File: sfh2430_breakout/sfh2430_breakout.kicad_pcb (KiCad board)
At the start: 2 copper layers, 45 x 60.3 mm, 118 parts, among them J1 Landing Pad, J10 Conn_01x01, J11 Conn_01x01, J12 Conn_01x01, J13 Conn_01x01, J2 Landing Pad, J3 Landing Pad, J4 Landing Pad, J5 Conn_01x10, J6 Conn_01x01, J7 Conn_01x01, J8 Conn_01x01, J9 Conn_01x01, U1 LTC2052IS_PBF

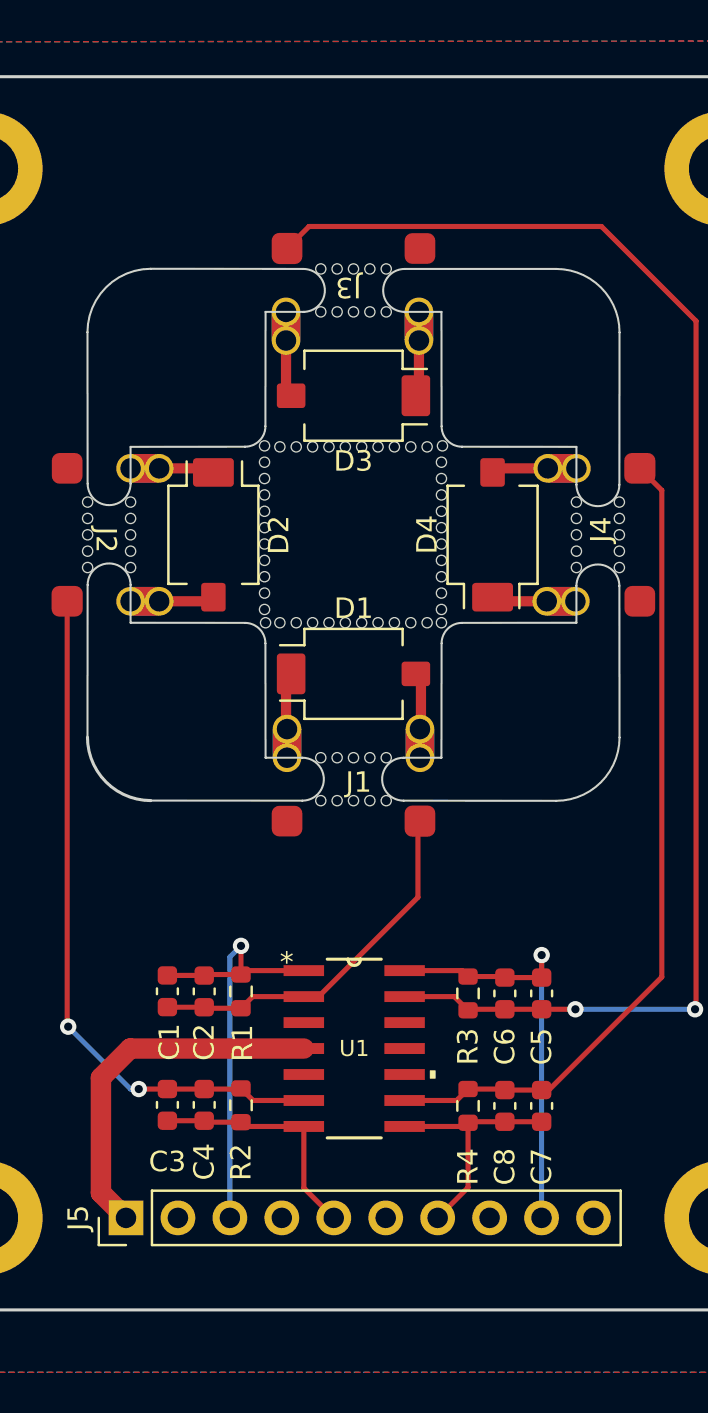
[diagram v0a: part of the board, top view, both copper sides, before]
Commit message: add math and decals
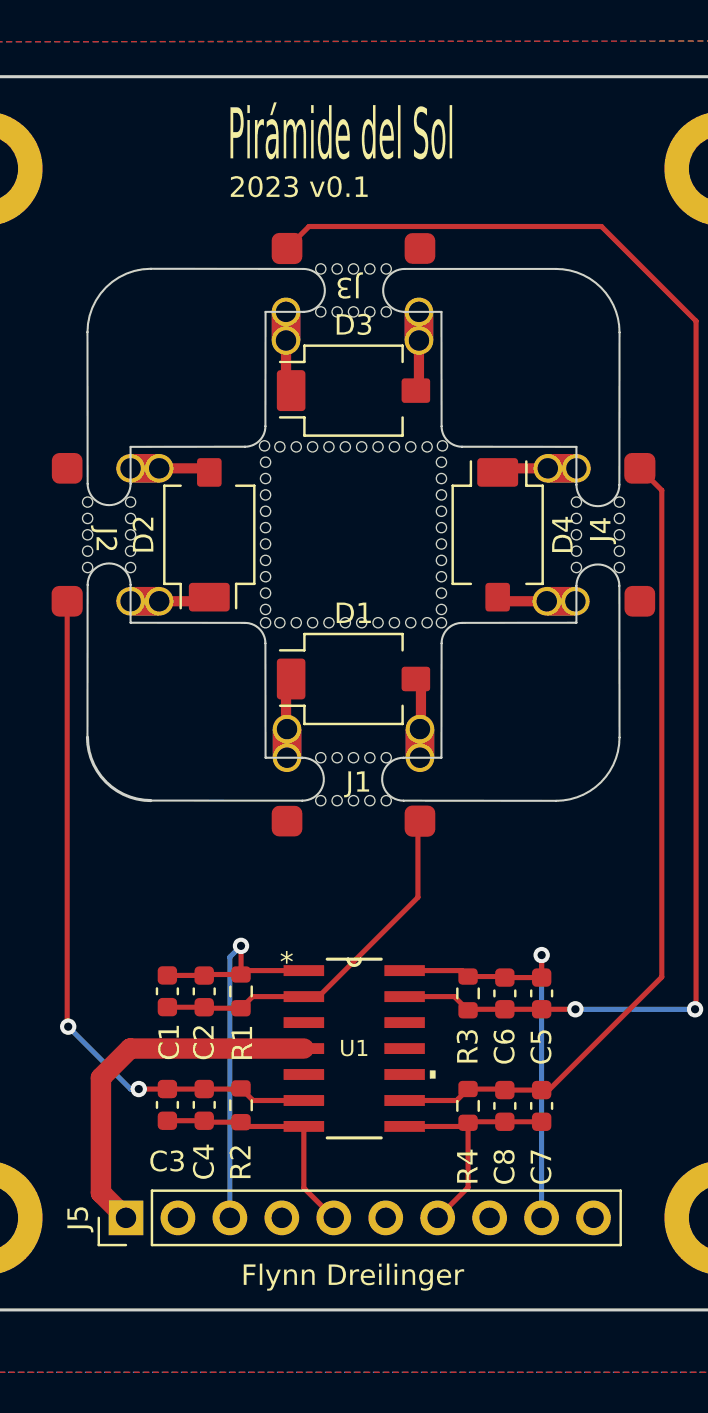
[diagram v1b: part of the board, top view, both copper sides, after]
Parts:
- added G***: LOGO, adcs:2ducks, B.Cu at (91.7, 67.8)
- added G***: LOGO, adcs:unlimited_ducks_2, B.Cu at (73.2, 51.9)
- added G***: LOGO, adcs:sats_pro_shop, B.Cu at (73.0, 91.0)
- added G***: LOGO, adcs:2ducks, B.Cu at (54.1, 68.2)
- R1, R2, R3, R4: value 1M -> 3.9k
- moved D1 0.25 mm to (72.8, 75.8)
- moved D3 0.25 mm to (72.8, 61.6), turned to 0 degrees
- moved D4 0.25 mm to (79.8, 68.7), turned to -90 degrees
- moved D2 0.20 mm to (65.8, 68.7), turned to 90 degrees
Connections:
- J10 pad 1: Net-(D3-A) -> Net-(D3-K)
- J11 pad 1: Net-(D3-K) -> Net-(D3-A)
- J12 pad 1: Net-(D4-A) -> Net-(D4-K)
- J13 pad 1: Net-(D4-K) -> Net-(D4-A)
- J6 pad 1: Net-(D1-A) -> Net-(D1-K)
- J7 pad 1: Net-(D1-K) -> Net-(D1-A)
- J8 pad 1: Net-(D2-A) -> Net-(D2-K)
- J9 pad 1: Net-(D2-K) -> Net-(D2-A)
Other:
- board text added: "2023 v0.1"
- board text added: "Flynn Dreilinger"
- board text added: "Pirámide del Sol"

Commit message: ordered sfh2430 breakout rev 0.1
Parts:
- removed the REF** at (74.4, 79.6)
- removed the REF** at (74.4, 57.8)
- removed the REF** at (77.1, 70.0)
- removed the REF** at (85.8, 67.9)
- removed the REF** at (71.2, 57.8)
- removed the REF** at (74.4, 81.7)
- removed the REF** at (77.1, 73.0)
- removed the REF** at (72.0, 55.7)
- removed the REF** at (76.4, 73.0)
- removed the REF** at (74.0, 64.4)
- removed the REF** at (77.1, 68.3)
- removed the REF** at (73.2, 64.4)
- removed the REF** at (69.2, 64.4)
- removed the REF** at (68.5, 70.8)
- removed the REF** at (68.5, 65.2)
- removed the REF** at (83.7, 67.9)
- removed the REF** at (75.6, 73.0)
- removed the REF** at (61.9, 69.5)
- removed the REF** at (70.0, 73.0)
- removed the REF** at (85.8, 69.5)
- removed the REF** at (73.6, 55.7)
- removed the REF** at (85.8, 67.1)
- removed the REF** at (73.2, 73.0)
- removed the REF** at (72.8, 57.8)
- removed the REF** at (68.5, 71.5)
- removed the REF** at (73.6, 81.7)
- removed the REF** at (68.5, 69.2)
- removed the REF** at (68.5, 66.0)
- removed the REF** at (72.4, 73.0)
- removed the REF** at (77.1, 66.0)
- removed the REF** at (61.9, 67.1)
- removed the REF** at (59.8, 69.5)
- removed the REF** at (70.0, 64.4)
- removed the REF** at (71.2, 79.6)
- removed the REF** at (71.6, 73.0)
- removed the REF** at (72.0, 79.6)
- removed the REF** at (77.2, 64.3)
- removed the REF** at (68.5, 72.3)
- removed the REF** at (71.2, 55.7)
- removed the REF** at (61.9, 70.3)
- removed the REF** at (77.1, 67.5)
- removed the REF** at (68.5, 70.0)
- removed the REF** at (72.0, 81.7)
- removed the REF** at (77.1, 66.8)
- removed the REF** at (77.1, 69.2)
- removed the REF** at (70.8, 64.4)
- removed the REF** at (73.6, 57.8)
- removed the REF** at (59.8, 67.1)
- removed the REF** at (68.5, 68.3)
- removed the REF** at (59.8, 70.3)
- removed the REF** at (74.0, 73.0)
- removed the REF** at (85.8, 70.3)
- removed the REF** at (83.7, 69.5)
- removed the REF** at (72.4, 64.4)
- removed the REF** at (77.1, 70.8)
- removed the REF** at (75.6, 64.4)
- removed the REF** at (70.8, 73.0)
- removed the REF** at (61.9, 68.7)
- removed the REF** at (68.5, 67.5)
- removed the REF** at (74.4, 55.7)
- removed the REF** at (71.6, 64.4)
- removed the REF** at (77.1, 72.3)
- removed the REF** at (59.8, 68.7)
- removed the REF** at (59.8, 67.9)
- removed the REF** at (83.7, 68.7)
- removed the REF** at (72.8, 81.7)
- removed the REF** at (72.8, 55.7)
- removed the REF** at (69.2, 73.0)
- removed the REF** at (73.6, 79.6)
- removed the REF** at (74.8, 73.0)
- removed the REF** at (68.5, 73.0)
- removed the REF** at (68.5, 66.8)
- removed the REF** at (72.0, 57.8)
- removed the REF** at (85.8, 68.7)
- removed the REF** at (61.9, 67.9)
- removed the REF** at (76.4, 64.4)
- removed the REF** at (83.7, 67.1)
- removed the REF** at (74.8, 64.4)
- removed the REF** at (71.2, 81.7)
- removed the REF** at (77.1, 65.2)
- removed the REF** at (83.7, 70.3)
- removed the REF** at (68.5, 64.3)
- removed the REF** at (77.1, 71.5)
- removed the REF** at (72.8, 79.6)
- added REF**: NPTH, NPTH, F.Cu at (87.0, 106.7)
- added REF**: NPTH, NPTH, F.Cu at (72.8, 115.7)
- added REF**: NPTH, NPTH, F.Cu at (66.7, 109.4)
- added REF**: NPTH, NPTH, F.Cu at (82.5, 114.9)
- added REF**: NPTH, NPTH, F.Cu at (75.7, 106.7)
- added REF**: NPTH, NPTH, F.Cu at (60.2, 106.7)
- added REF**: NPTH, NPTH, F.Cu at (58.6, 109.4)
- added REF**: NPTH, NPTH, F.Cu at (77.2, 106.7)
- added REF**: NPTH, NPTH, F.Cu at (63.1, 110.0)
- added REF**: NPTH, NPTH, F.Cu at (61.0, 106.7)
- added REF**: NPTH, NPTH, F.Cu at (77.2, 109.4)
- added REF**: NPTH, NPTH, F.Cu at (68.3, 109.4)
- added REF**: NPTH, NPTH, F.Cu at (79.7, 106.7)
- added REF**: NPTH, NPTH, F.Cu at (57.0, 109.4)
- added REF**: NPTH, NPTH, F.Cu at (84.5, 106.7)
- added REF**: NPTH, NPTH, F.Cu at (63.1, 114.8)
- added REF**: NPTH, NPTH, F.Cu at (87.8, 106.7)
- added REF**: NPTH, NPTH, F.Cu at (89.3, 106.7)
- added REF**: NPTH, NPTH, F.Cu at (78.8, 106.7)
- added REF**: NPTH, NPTH, F.Cu at (67.5, 109.4)
- added REF**: NPTH, NPTH, F.Cu at (72.8, 110.9)
- added REF**: NPTH, NPTH, F.Cu at (58.6, 106.7)
- added REF**: NPTH, NPTH, F.Cu at (82.5, 115.7)
- added REF**: NPTH, NPTH, F.Cu at (82.5, 110.9)
- added REF**: NPTH, NPTH, F.Cu at (76.4, 109.4)
- added REF**: NPTH, NPTH, F.Cu at (79.6, 109.4)
- added REF**: NPTH, NPTH, F.Cu at (90.2, 106.7)
- added REF**: NPTH, NPTH, F.Cu at (66.8, 106.7)
- added REF**: NPTH, NPTH, F.Cu at (84.5, 109.5)
- added REF**: NPTH, NPTH, F.Cu at (86.9, 109.5)
- added REF**: NPTH, NPTH, F.Cu at (82.5, 113.3)
- added REF**: NPTH, NPTH, F.Cu at (60.2, 109.4)
- added REF**: NPTH, NPTH, F.Cu at (63.1, 114.0)
- added REF**: NPTH, NPTH, F.Cu at (63.1, 111.6)
- added REF**: NPTH, NPTH, F.Cu at (57.8, 109.4)
- added REF**: NPTH, NPTH, F.Cu at (82.5, 110.1)
- added REF**: NPTH, NPTH, F.Cu at (85.3, 109.5)
- added REF**: NPTH, NPTH, F.Cu at (72.8, 114.9)
- added REF**: NPTH, NPTH, F.Cu at (69.9, 109.4)
- added REF**: NPTH, NPTH, F.Cu at (74.8, 109.4)
- added REF**: NPTH, NPTH, F.Cu at (69.2, 106.7)
- added REF**: NPTH, NPTH, F.Cu at (57.0, 106.7)
- added REF**: NPTH, NPTH, F.Cu at (63.1, 113.2)
- added REF**: NPTH, NPTH, F.Cu at (57.9, 106.7)
- added REF**: NPTH, NPTH, F.Cu at (66.0, 106.7)
- added REF**: NPTH, NPTH, F.Cu at (72.8, 110.1)
- added REF**: NPTH, NPTH, F.Cu at (56.2, 106.7)
- added REF**: NPTH, NPTH, F.Cu at (55.5, 106.7)
- added REF**: NPTH, NPTH, F.Cu at (74.8, 106.7)
- added REF**: NPTH, NPTH, F.Cu at (65.2, 106.7)
- added REF**: NPTH, NPTH, F.Cu at (69.1, 109.4)
- added REF**: NPTH, NPTH, F.Cu at (68.3, 106.7)
- added REF**: NPTH, NPTH, F.Cu at (88.5, 106.7)
- added REF**: NPTH, NPTH, F.Cu at (86.2, 106.7)
- added REF**: NPTH, NPTH, F.Cu at (87.7, 109.5)
- added REF**: NPTH, NPTH, F.Cu at (72.8, 111.7)
- added REF**: NPTH, NPTH, F.Cu at (55.4, 109.4)
- added REF**: NPTH, NPTH, F.Cu at (72.8, 114.1)
- added REF**: NPTH, NPTH, F.Cu at (82.5, 114.1)
- added REF**: NPTH, NPTH, F.Cu at (78.0, 106.7)
- added REF**: NPTH, NPTH, F.Cu at (63.1, 110.8)
- added REF**: NPTH, NPTH, F.Cu at (59.5, 106.7)
- added REF**: NPTH, NPTH, F.Cu at (65.1, 109.4)
- added REF**: NPTH, NPTH, F.Cu at (59.4, 109.4)
- added REF**: NPTH, NPTH, F.Cu at (88.5, 109.5)
- added REF**: NPTH, NPTH, F.Cu at (70.0, 106.7)
- added REF**: NPTH, NPTH, F.Cu at (82.5, 111.7)
- added REF**: NPTH, NPTH, F.Cu at (61.0, 109.4)
- added REF**: NPTH, NPTH, F.Cu at (80.4, 109.4)
- added REF**: NPTH, NPTH, F.Cu at (63.1, 112.4)
- added REF**: NPTH, NPTH, F.Cu at (76.5, 106.7)
- added REF**: NPTH, NPTH, F.Cu at (63.1, 115.6)
- added REF**: NPTH, NPTH, F.Cu at (80.5, 106.7)
- added REF**: NPTH, NPTH, F.Cu at (56.2, 109.4)
- added REF**: NPTH, NPTH, F.Cu at (70.8, 106.7)
- added REF**: NPTH, NPTH, F.Cu at (70.7, 109.4)
- added REF**: NPTH, NPTH, F.Cu at (78.0, 109.4)
- added REF**: NPTH, NPTH, F.Cu at (90.1, 109.5)
- added REF**: NPTH, NPTH, F.Cu at (65.9, 109.4)
- added REF**: NPTH, NPTH, F.Cu at (86.1, 109.5)
- added REF**: NPTH, NPTH, F.Cu at (72.8, 112.5)
- added REF**: NPTH, NPTH, F.Cu at (89.3, 109.5)
- added REF**: NPTH, NPTH, F.Cu at (67.5, 106.7)
- added REF**: NPTH, NPTH, F.Cu at (78.8, 109.4)
- added REF**: NPTH, NPTH, F.Cu at (85.3, 106.7)
- added REF**: NPTH, NPTH, F.Cu at (75.6, 109.4)
- added REF**: NPTH, NPTH, F.Cu at (82.5, 112.5)
- added REF**: NPTH, NPTH, F.Cu at (72.8, 113.3)
- D1, D2, D3, D4: footprint OptoDevice:Osram_SFH2430 -> adcs:Osram_SFH2430
- moved J11 59.5 mm to (64.8, 116.2), turned to -90 degrees
- moved J10 58.4 mm to (71.2, 116.2), turned to -90 degrees
- moved D3 50.9 mm to (68.0, 112.3), turned to 180 degrees
- moved J12 50.8 mm to (80.9, 116.2), turned to -90 degrees
- moved J9 50.0 mm to (55.0, 114.8), turned to 90 degrees
- moved J13 45.2 mm to (74.4, 116.2), turned to -90 degrees
- moved D2 44.3 mm to (58.2, 112.3), turned to 180 degrees
- moved D4 43.7 mm to (77.7, 112.3), turned to 180 degrees
- moved J8 42.9 mm to (61.5, 114.8), turned to 90 degrees
- moved D1 39.4 mm to (87.3, 112.3), turned to 180 degrees
- moved J6 39.4 mm to (90.5, 114.8)
- moved J7 39.4 mm to (84.0, 114.8)
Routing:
- net GND: vias 0 -> 2
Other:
- board size 45 x 60.3 mm -> 45 x 69.9 mm
- board text added: "A"
- board text added: "B"
- board text added: "C"
- board text added: "D"

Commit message: sfh2400 v2 (flex PCB)
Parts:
- removed G*** (x2): LOGO, adcs:2ducks
- removed G***: LOGO, adcs:unlimited_ducks_2
- removed G***: LOGO, adcs:sats_pro_shop
- removed H3: MountingHole_Pad, MountingHole:MountingHole_3.2mm_M3_DIN965_Pad
- removed J10, J11, J12, J13, J6, J7, J8, J9: Conn_01x01, adcs:castellated_05mm
- removed J2, J3, J4: Landing Pad, adcs:photodiode_landing_pad
- removed J5: Conn_01x10, Connector_PinHeader_2.54mm:PinHeader_1x10_P2.54mm_Vertical
- removed REF** (x88): NPTH, NPTH
- added locked: MountingHole_Pad, MountingHole:MountingHole_2.2mm_M2_DIN965_Pad_TopBottom, F.Cu at (113.0, 94.0)
- H1, H2, H4: footprint MountingHole:MountingHole_3.2mm_M3_DIN965_Pad -> MountingHole:MountingHole_2.2mm_M2_DIN965_Pad_TopBottom
- J1: value Landing Pad -> Conn_01x06; footprint adcs:photodiode_landing_pad -> sapling:MOLEX_2053380006
- moved H1 57.1 mm to (92.2, 94.0)
- moved D3 54.9 mm to (122.3, 104.5), turned to -90 degrees
- moved J1 42.2 mm to (102.5, 112.7), turned to 180 degrees
- moved H2 38.6 mm to (92.2, 111.8)
- moved C3 32.1 mm to (94.9, 104.1)
- moved C1 32.0 mm to (94.9, 98.3)
- moved C4 31.7 mm to (96.3, 104.1)
- moved C2 31.7 mm to (96.3, 98.3)
- moved D1 31.6 mm to (102.5, 84.7), turned to 0 degrees
- moved R2 31.4 mm to (97.8, 104.1)
- moved R1 31.3 mm to (97.8, 98.3)
- moved U1 30.5 mm to (102.5, 101.2)
- moved R4 29.8 mm to (107.2, 104.1)
- moved R3 29.7 mm to (107.2, 98.3)
- moved C8 29.4 mm to (108.7, 104.1)
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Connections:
- C1 pad 1: Net-(J1-Pin_2) -> /Photodiode 1/IN-
- C1 pad 2: /OUTA -> /OUT1
- C2 pad 1: Net-(J1-Pin_2) -> /Photodiode 1/IN-
- C2 pad 2: /OUTA -> /OUT1
- C3 pad 1: Net-(J2-Pin_2) -> /Photodiode 2/IN-
- C3 pad 2: /OUTB -> /OUT2
- C4 pad 1: Net-(J2-Pin_2) -> /Photodiode 2/IN-
- C4 pad 2: /OUTB -> /OUT2
- C5 pad 1: Net-(J3-Pin_2) -> /Photodiode 4/IN-
- C5 pad 2: /OUTD -> /OUT4
- C6 pad 1: Net-(J3-Pin_2) -> /Photodiode 4/IN-
- C6 pad 2: /OUTD -> /OUT4
- C7 pad 1: Net-(J4-Pin_2) -> /Photodiode 3/IN-
- C7 pad 2: /OUTC -> /OUT3
- C8 pad 1: Net-(J4-Pin_2) -> /Photodiode 3/IN-
- C8 pad 2: /OUTC -> /OUT3
- D1 pad 1: Net-(D1-K) -> /Photodiode 1/IN-
- D1 pad 2: Net-(D1-A) -> GND
- D2 pad 1: Net-(D2-K) -> /Photodiode 2/IN-
- D2 pad 2: Net-(D2-A) -> GND
- D3 pad 1: Net-(D3-K) -> /Photodiode 4/IN-
- D3 pad 2: Net-(D3-A) -> GND
- D4 pad 1: Net-(D4-K) -> /Photodiode 3/IN-
- D4 pad 2: Net-(D4-A) -> GND
- J1 pad 2: Net-(J1-Pin_2) -> /OUT2
- R1 pad 1: Net-(J1-Pin_2) -> /Photodiode 1/IN-
- R1 pad 2: /OUTA -> /OUT1
- R2 pad 1: Net-(J2-Pin_2) -> /Photodiode 2/IN-
- R2 pad 2: /OUTB -> /OUT2
- R3 pad 1: Net-(J3-Pin_2) -> /Photodiode 4/IN-
- R3 pad 2: /OUTD -> /OUT4
- R4 pad 1: Net-(J4-Pin_2) -> /Photodiode 3/IN-
- R4 pad 2: /OUTC -> /OUT3
- U1 pad 1: /OUTA -> /OUT1
- U1 pad 13: Net-(J3-Pin_2) -> /Photodiode 4/IN-
- U1 pad 14: /OUTD -> /OUT4
- U1 pad 2: Net-(J1-Pin_2) -> /Photodiode 1/IN-
- U1 pad 6: Net-(J2-Pin_2) -> /Photodiode 2/IN-
- U1 pad 7: /OUTB -> /OUT2
- U1 pad 8: /OUTC -> /OUT3
- U1 pad 9: Net-(J4-Pin_2) -> /Photodiode 3/IN-
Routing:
- net Net-(J3-Pin_2): track 70.5 -> 0.00 mm, vias 2 -> 0
- net Net-(J4-Pin_2): track 40.4 -> 0.00 mm
- net Net-(J2-Pin_2): track 33.9 -> 0.00 mm, vias 2 -> 0
- net /Photodiode 3/IN-: track 0.00 -> 32.7 mm
- net /Photodiode 1/IN-: track 0.00 -> 28.0 mm
- net /Photodiode 4/IN-: track 0.00 -> 22.0 mm
- net /OUTA: track 21.7 -> 0.00 mm, vias 1 -> 0
- net /OUTD: track 20.8 -> 0.00 mm, vias 1 -> 0
- net /Photodiode 2/IN-: track 0.00 -> 19.2 mm
- net /OUT1: track 0.00 -> 19.0 mm
- net Net-(J1-Pin_2): track 18.3 -> 0.00 mm
- net /OUT4: track 0.00 -> 18.2 mm
- net /OUTC: track 12.1 -> 0.00 mm
- net /OUTB: track 11.9 -> 0.00 mm
- net /OUT3: track 0.00 -> 9.79 mm
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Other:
- board size 45 x 69.9 mm -> 44.7 x 44.7 mm
- board text removed: "2023 v0.1"
- board text removed: "A"
- board text removed: "B"
- board text removed: "C"
- board text removed: "D"
- board text removed: "Flynn Dreilinger"
- board text removed: "Pirámide del Sol"

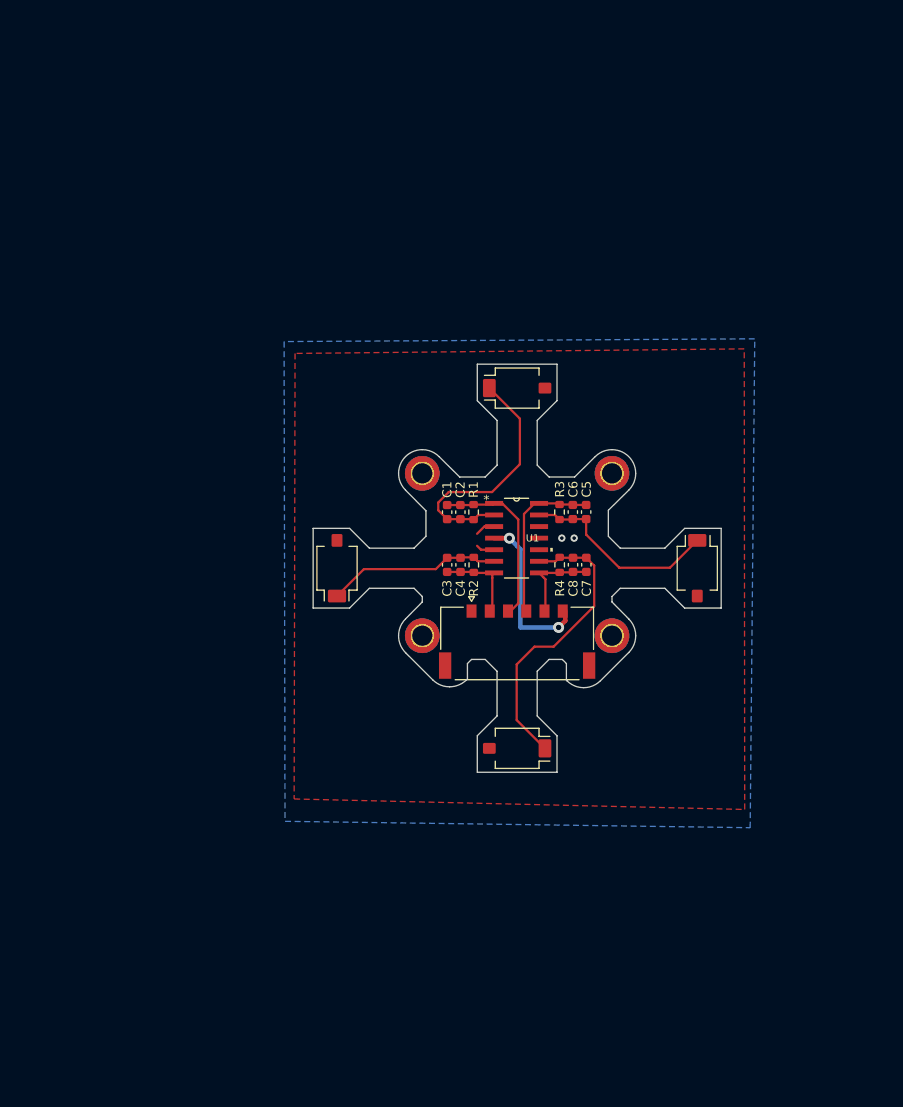
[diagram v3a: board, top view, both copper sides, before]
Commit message: ffc/fpc pyramid
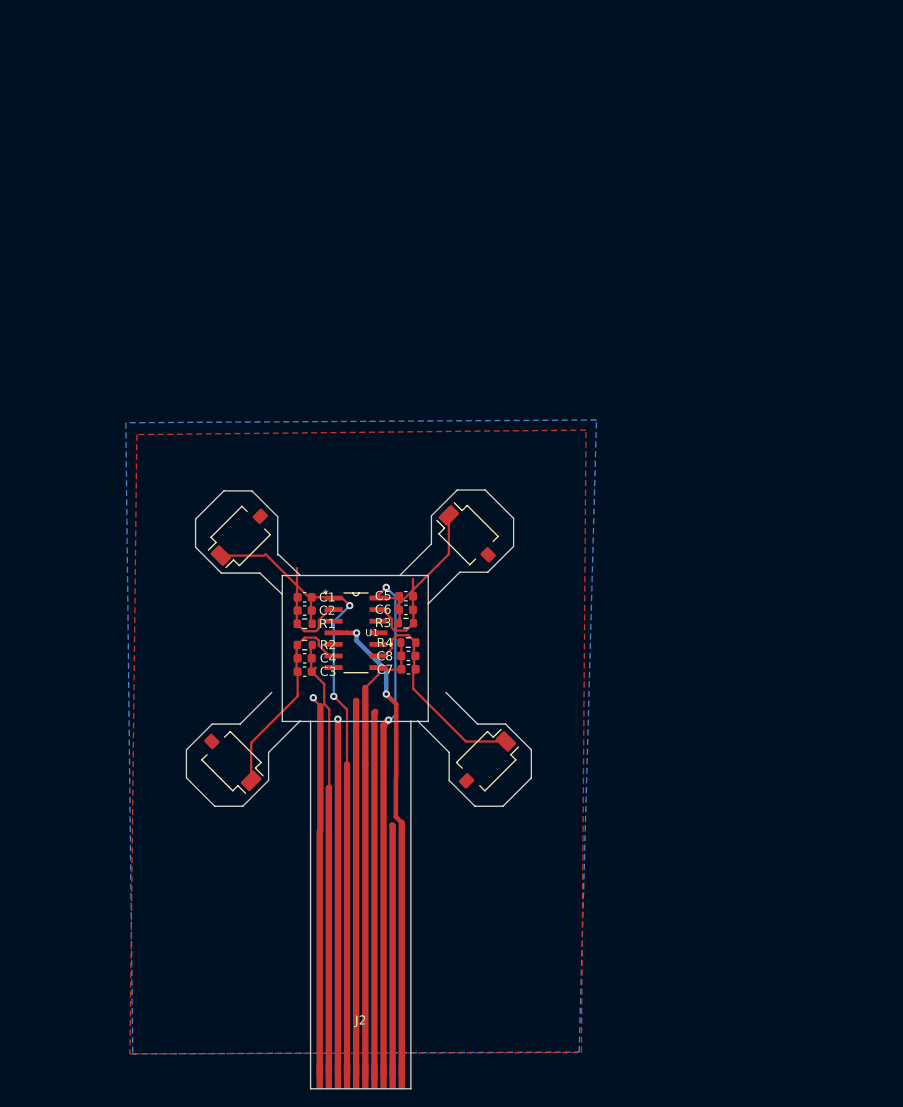
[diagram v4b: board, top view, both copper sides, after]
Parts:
- removed H1, H2, H4, locked: MountingHole_Pad, MountingHole:MountingHole_2.2mm_M2_DIN965_Pad_TopBottom
- removed J1: Conn_01x06, sapling:MOLEX_2053380006
- added J2: Conn_01x10, adcs:10pin_1mm_pitch_flat_flex, F.Cu at (85.4, 160.2)
- moved D1 34.4 mm to (72.2, 100.9), turned to 45 degrees
- moved D3 25.3 mm to (97.2, 100.8), turned to -45 degrees
- moved D2 24.1 mm to (71.2, 125.6), turned to 135 degrees
- moved C7 22.6 mm to (90.6, 115.5), turned to 180 degrees
- moved R1 22.2 mm to (79.3, 110.5), turned to 0 degrees
- moved C5 21.8 mm to (90.4, 107.5), turned to 180 degrees
- moved C6 21.2 mm to (90.4, 109.0), turned to 180 degrees
- moved R3 20.8 mm to (90.4, 110.5), turned to 180 degrees
- moved C8 20.6 mm to (90.6, 114.1), turned to 180 degrees
- moved R2 20.5 mm to (79.3, 112.9), turned to 0 degrees
- moved U1 20.4 mm to (84.9, 111.5)
- moved C2 20.2 mm to (79.3, 109.1), turned to 0 degrees
- moved C4 19.9 mm to (79.3, 114.3), turned to 0 degrees
- moved C3 19.5 mm to (79.3, 115.8), turned to 0 degrees
- moved R4 18.7 mm to (90.6, 112.6), turned to 180 degrees
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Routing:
- net GND: track 4.24 -> 191.0 mm
- net /OUT4: track 18.2 -> 62.0 mm, vias 0 -> 2
- net /OUT1: track 19.0 -> 61.9 mm, vias 0 -> 2
- net /OUT3: track 9.79 -> 50.8 mm
- net /OUT2: track 9.46 -> 48.8 mm
- net +3V3: track 18.2 -> 53.2 mm
- net /Photodiode 3/IN-: track 32.7 -> 23.6 mm
- net /Photodiode 1/IN-: track 28.0 -> 23.2 mm
- net /Photodiode 2/IN-: track 19.2 -> 22.6 mm
- net /Photodiode 4/IN-: track 22.0 -> 23.1 mm
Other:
- board size 44.7 x 44.7 mm -> 37.8 x 65.6 mm
